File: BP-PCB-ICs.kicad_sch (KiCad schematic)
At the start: 32 parts, among them IC1 LMT84DCKT, Q1 SSM6K514NU,LF, Q2 SSM6K514NU,LF, Q3 SSM6K514NU,LF, Q4 SSM6K514NU,LF, U1 SN74CB3Q3257DBQR, U2 SN74CB3Q3257DBQR, U3 LTC4361CTS8-2TRMPBF, U4 LTC4380IDD-4-PBF, U5 LTC4361CTS8-2TRMPBF

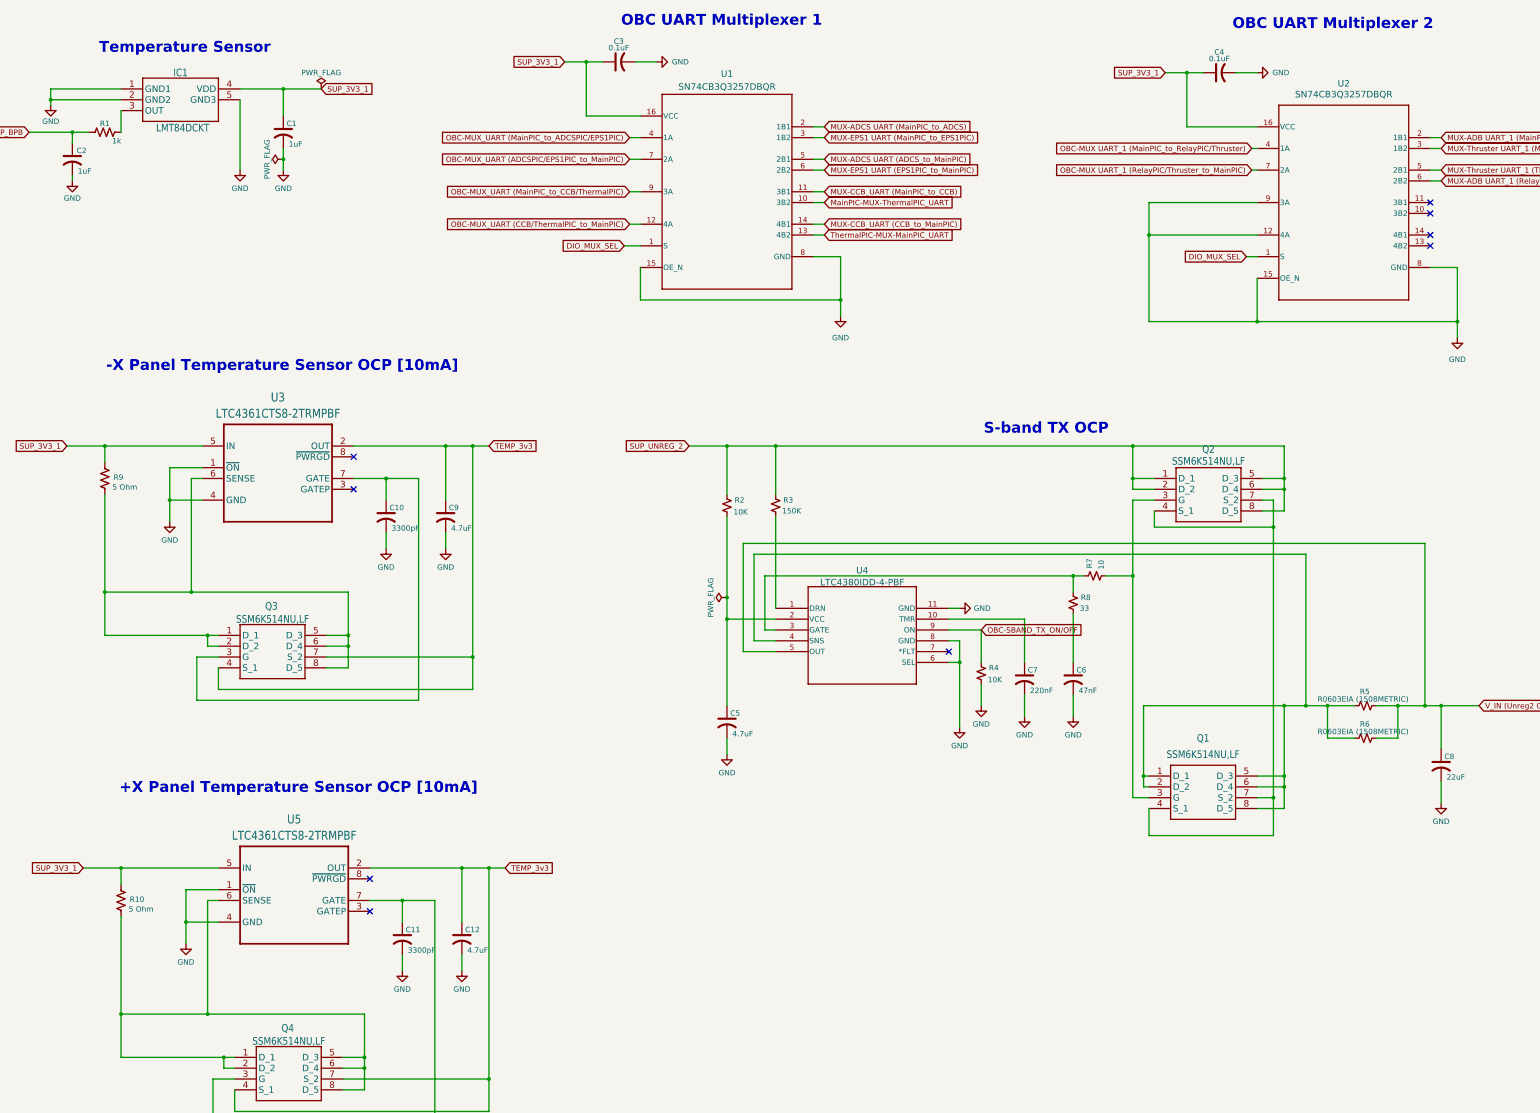
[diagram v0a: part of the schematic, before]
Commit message: Fixed errors in schematics
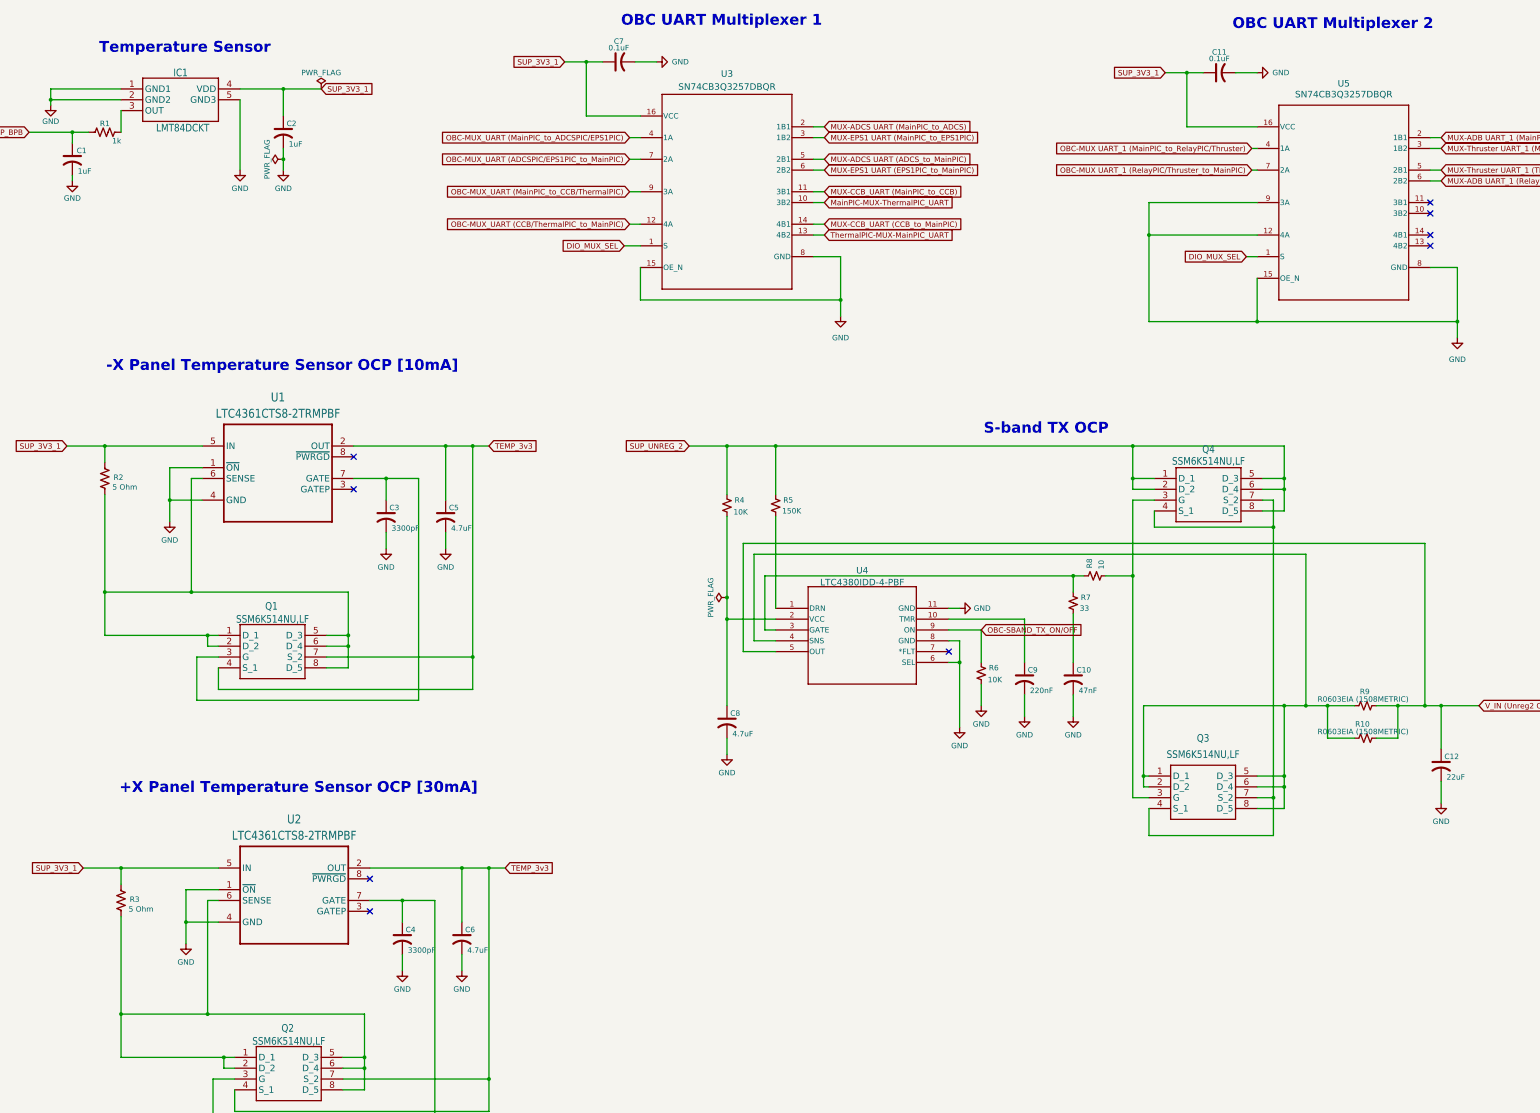
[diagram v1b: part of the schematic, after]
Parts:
- C1: renamed from C2; footprint (none) -> Capacitor_SMD:C_0805_2012Metric
- C10: renamed from C6; footprint (none) -> Capacitor_SMD:C_0805_2012Metric
- C11: renamed from C4; footprint (none) -> Capacitor_SMD:C_0805_2012Metric
- C12: renamed from C8; footprint (none) -> Capacitor_SMD:C_0805_2012Metric
- C2: renamed from C1; footprint (none) -> Capacitor_SMD:C_0805_2012Metric
- C3: renamed from C10; footprint (none) -> Capacitor_SMD:C_0805_2012Metric
- C4: renamed from C11; footprint (none) -> Capacitor_SMD:C_0805_2012Metric
- C5: renamed from C9; footprint (none) -> Capacitor_SMD:C_0805_2012Metric
- C6: renamed from C12; footprint (none) -> Capacitor_SMD:C_0805_2012Metric
- C7: renamed from C3; footprint (none) -> Capacitor_SMD:C_0805_2012Metric
- C8: renamed from C5; footprint (none) -> Capacitor_SMD:C_0805_2012Metric
- C9: renamed from C7; footprint (none) -> Capacitor_SMD:C_0805_2012Metric
- R1: footprint (none) -> Resistor_SMD:R_0805_2012Metric
- R10: renamed from R6; footprint (none) -> Resistor_SMD:R_0805_2012Metric
- R2: renamed from R9; footprint (none) -> Resistor_SMD:R_0805_2012Metric
- R3: renamed from R10; footprint (none) -> Resistor_SMD:R_0805_2012Metric
- R4: renamed from R2; footprint Resistor_SMD:R_0603_1608Metric -> Resistor_SMD:R_0805_2012Metric
- R5: renamed from R3; footprint (none) -> Resistor_SMD:R_0805_2012Metric
- R6: renamed from R4; footprint (none) -> Resistor_SMD:R_0805_2012Metric
- R7: renamed from R8; footprint (none) -> Resistor_SMD:R_0805_2012Metric
- R8: renamed from R7; footprint (none) -> Resistor_SMD:R_0805_2012Metric
- R9: renamed from R5; footprint (none) -> Resistor_SMD:R_0805_2012Metric
- U4: footprint DD_10_ADI -> Custom-Footprints:LTC4380IDD-4#PBF
- renumbered Q3 to Q1, Q4 to Q2, Q1 to Q3, Q2 to Q4, U3 to U1, U5 to U2, U1 to U3, U2 to U5
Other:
- note added: "+X Panel Temperature Sensor OCP [30mA]"
- note removed: "+X Panel Temperature Sensor OCP [10mA]"
